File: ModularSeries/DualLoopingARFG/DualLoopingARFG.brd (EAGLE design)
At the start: 91.4 x 47.9 mm, 63 parts, among them IC1 TL0X4_DIP, IC2 TL0X4_DIP, P1 2XWIREPAD, P2 2XWIREPAD, P3 2XWIREPAD, P4 2XWIREPAD, Q1 2N3904, Q2 2N3904

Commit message: Library updated, variants consolidated
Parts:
- IC1, IC2: value TL0X4_DIP -> (none)
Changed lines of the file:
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@@
 <attribute name="NAME" x="37.973" y="17.145" size="0.8128" layer="25" font="vector" ratio="20" rot="R90" align="bottom-center"/>
 </element>
-<element name="IC2" library="ElectricNoodleBox" package="DIL14" package3d_urn="urn:adsk.eagle:package:16407/2" value="TL0X4_DIP" x="29.21" y="24.13" smashed="yes">
+<element name="IC2" library="ElectricNoodleBox" package="DIL14" package3d_urn="urn:adsk.eagle:package:16407/2" value="" x="29.21" y="24.13" smashed="yes">
 <attribute name="NAME" x="19.939" y="21.082" size="1.27" layer="25" ratio="10" rot="R90"/>
 <attribute name="VALUE" x="22.479" y="23.495" size="1.27" layer="27" ratio="10"/>
@@
 <attribute name="VALUE" x="53.34" y="47.752" size="0.6096" layer="27" font="vector" ratio="20" rot="R180"/>
 </element>
-<element name="IC1" library="ElectricNoodleBox" package="DIL14" package3d_urn="urn:adsk.eagle:package:16407/2" value="TL0X4_DIP" x="66.04" y="24.13" smashed="yes">
+<element name="IC1" library="ElectricNoodleBox" package="DIL14" package3d_urn="urn:adsk.eagle:package:16407/2" value="" x="66.04" y="24.13" smashed="yes">
 <attribute name="NAME" x="56.769" y="21.082" size="1.27" layer="25" ratio="10" rot="R90"/>
 <attribute name="VALUE" x="59.309" y="23.495" size="1.27" layer="27" ratio="10"/>

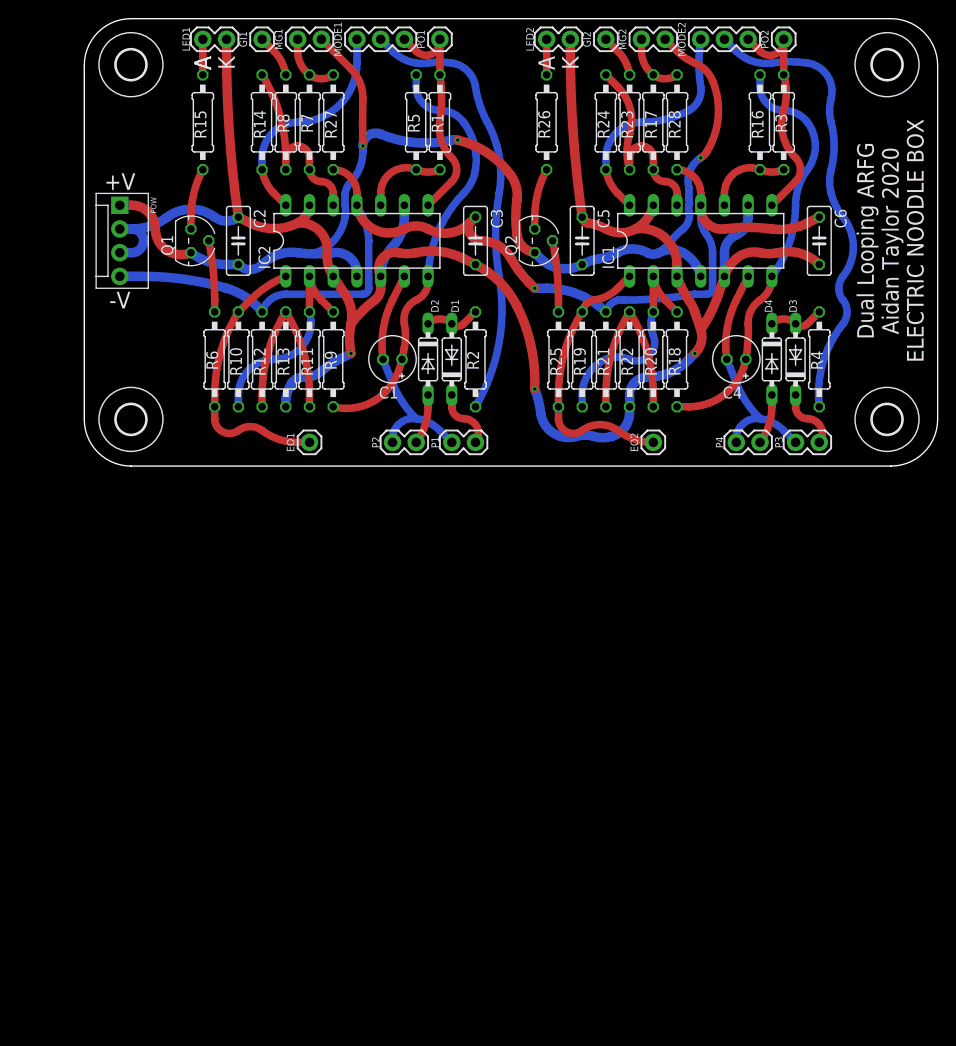
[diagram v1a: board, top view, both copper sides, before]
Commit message: Updates to ARFG schematic - not included in layout yet
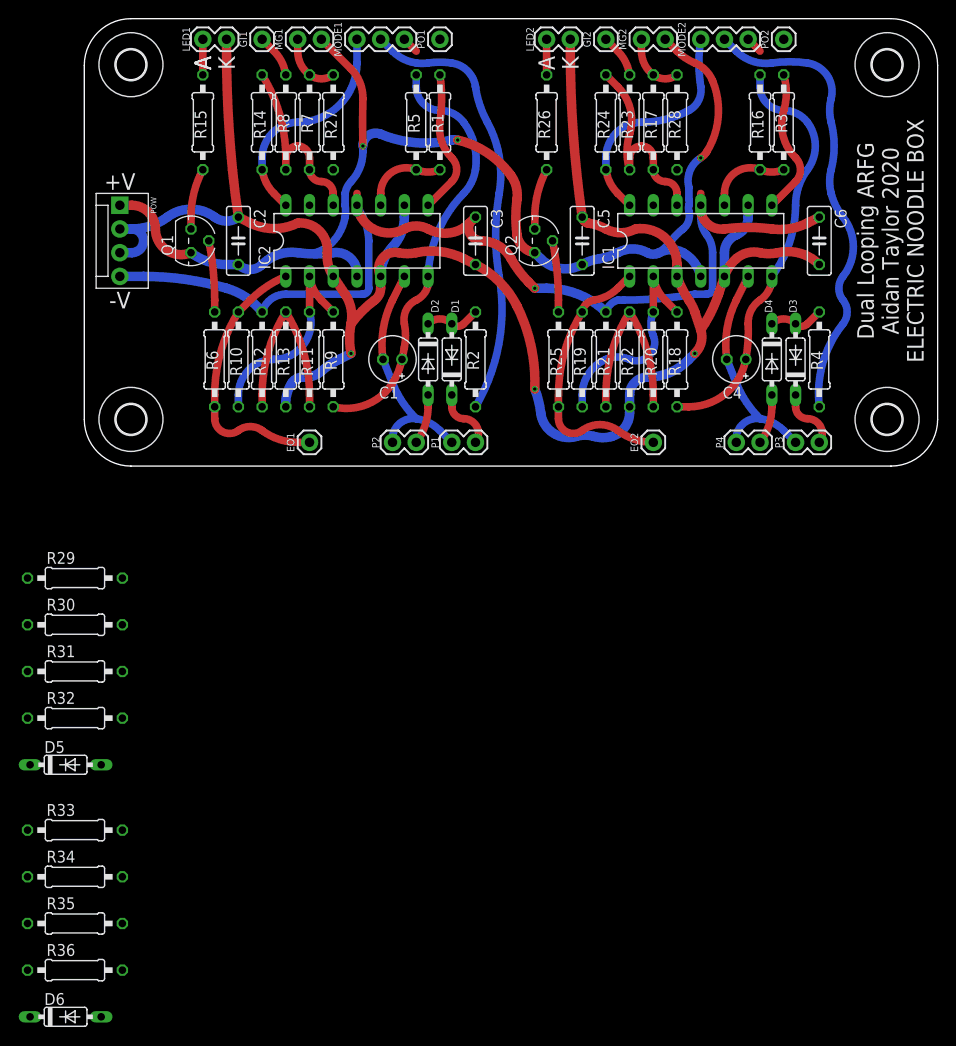
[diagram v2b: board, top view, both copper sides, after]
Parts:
- added D5, D6: BAT85, ElectricNoodleBox:DO35-7
- added R29, R33: 140K, rcl:0207/10
- added R30, R34: 100K, rcl:0207/10
- added R31, R35: 14K, rcl:0207/10
- added R32, R36: 10K, rcl:0207/10
- R8: value 150K -> 75K
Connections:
- new net N$33: IC2.13, R29.1, R30.1
- new net N$34: D5.C, PO1.1, R31.1, R32.2
- new net N$35: IC1.13, R33.1, R34.1
- new net N$36: D6.C, PO2.1, R35.1, R36.2
- net +12V: now also R29.2, R33.2
- net -12V: no longer R27.2, R28.2
- net GNDA: now also D5.A, D6.A, R27.2, R28.2, R30.2, R32.1, R34.2, R36.1; no longer IC1.13, IC2.13
- net N$1: now also R31.2; no longer PO1.1
- net N$17: now also R35.2; no longer PO2.1
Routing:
- net -12V: track 114.3 -> 107.2 mm
- net N$17: track 23.6 -> 17.0 mm
- net N$1: track 23.7 -> 17.0 mm
- net GNDA: track 206.5 -> 201.1 mm
